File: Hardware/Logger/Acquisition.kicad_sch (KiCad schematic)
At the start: 9 parts, among them J1 Conn_Coaxial, J2 Conn_Coaxial, J3 Conn_Coaxial, J4 Conn_Coaxial, J7 DB9_Female_MountingHoles

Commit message: fix #41
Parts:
- added Q5, Q6, Q7, Q8: BC848, Package_TO_SOT_SMD:SOT-23, symbol Transistor_BJT:BC848
- added R10, R35, R38, R39: 8k2, Resistor_SMD:R_0805_2012Metric, symbol Device:R
- added R36, R37: 100R, Resistor_SMD:R_0805_2012Metric, symbol Device:R
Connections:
- net ANALOG_IN_1: now also Q5.3 (C); no longer R9.2
- net ANALOG_IN_2: now also Q6.3 (C); no longer R100R1.2
- net ANALOG_IN_3: now also Q7.3 (C); no longer R11.2
- net ANALOG_IN_4: now also Q8.3 (C); no longer R12.2
- net EXT_RX: now also R36.1; no longer J7.2
- net EXT_TX: now also R37.1; no longer J7.3
- net GND: now also Q5.2 (E), Q6.2 (E), Q7.2 (E), Q8.2 (E), R10.1, R35.1, R38.1, R39.1
- new net: Q5.1 (B), R10.2, R9.2
- new net: Q6.1 (B), R100R1.2, R35.2
- new net: J7.2, R36.2
- new net: J7.3, R37.2
- new net: Q7.1 (B), R11.2, R38.2
- new net: Q8.1 (B), R12.2, R39.2
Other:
- moved on the sheet: J1, J2, J3, J4, J7, R100R1, R11, R12, R9

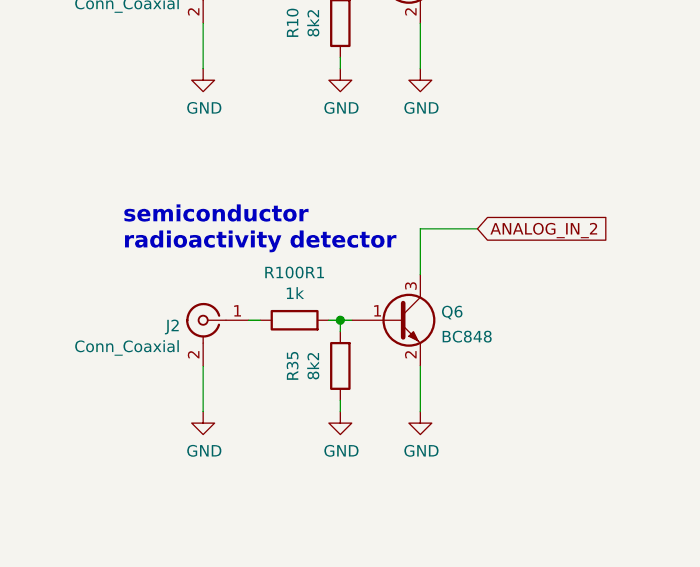
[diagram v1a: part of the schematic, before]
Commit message: cleanup after transition to KiCad6
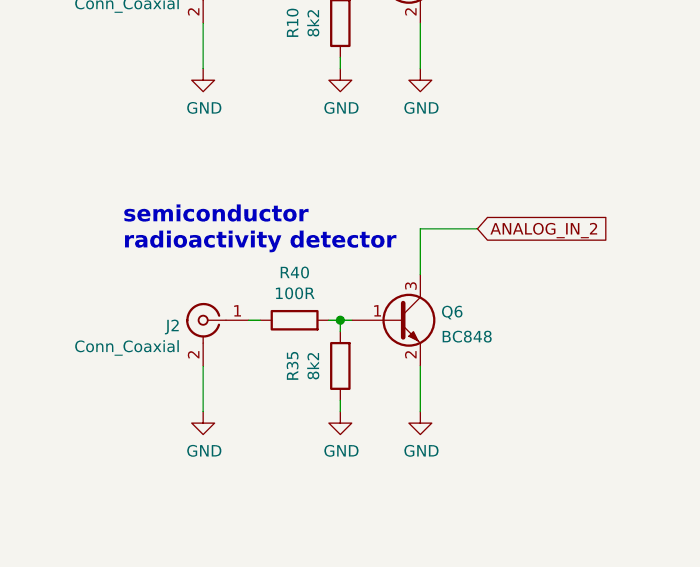
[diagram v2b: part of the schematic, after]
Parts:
- removed R100R1: 1k, Resistor_SMD:R_0805_2012Metric, symbol Device:R
- added R40: 100R, Resistor_SMD:R_0805_2012Metric, symbol Device:R
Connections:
- net at J2.1 (In): now also R40.1
- net at Q6.1 (B), R35.2: now also R40.2
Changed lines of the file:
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@@
   (symbol (lib_id "Device:R") (at 53.34 69.85 90) (unit 1)
     (in_bom yes) (on_board yes)
-    (property "Reference" "R100R1" (id 0) (at 53.34 64.5922 90))
-    (property "Value" "1k" (id 1) (at 53.34 66.9036 90))
+    (property "Reference" "R40" (id 0) (at 53.34 64.5922 90))
+    (property "Value" "100R" (id 1) (at 53.34 66.9036 90))
     (property "Footprint" "Resistor_SMD:R_0805_2012Metric" (id 2) (at 53.34 71.628 90)
       (effects (font (size 1.27 1.27)) hide)

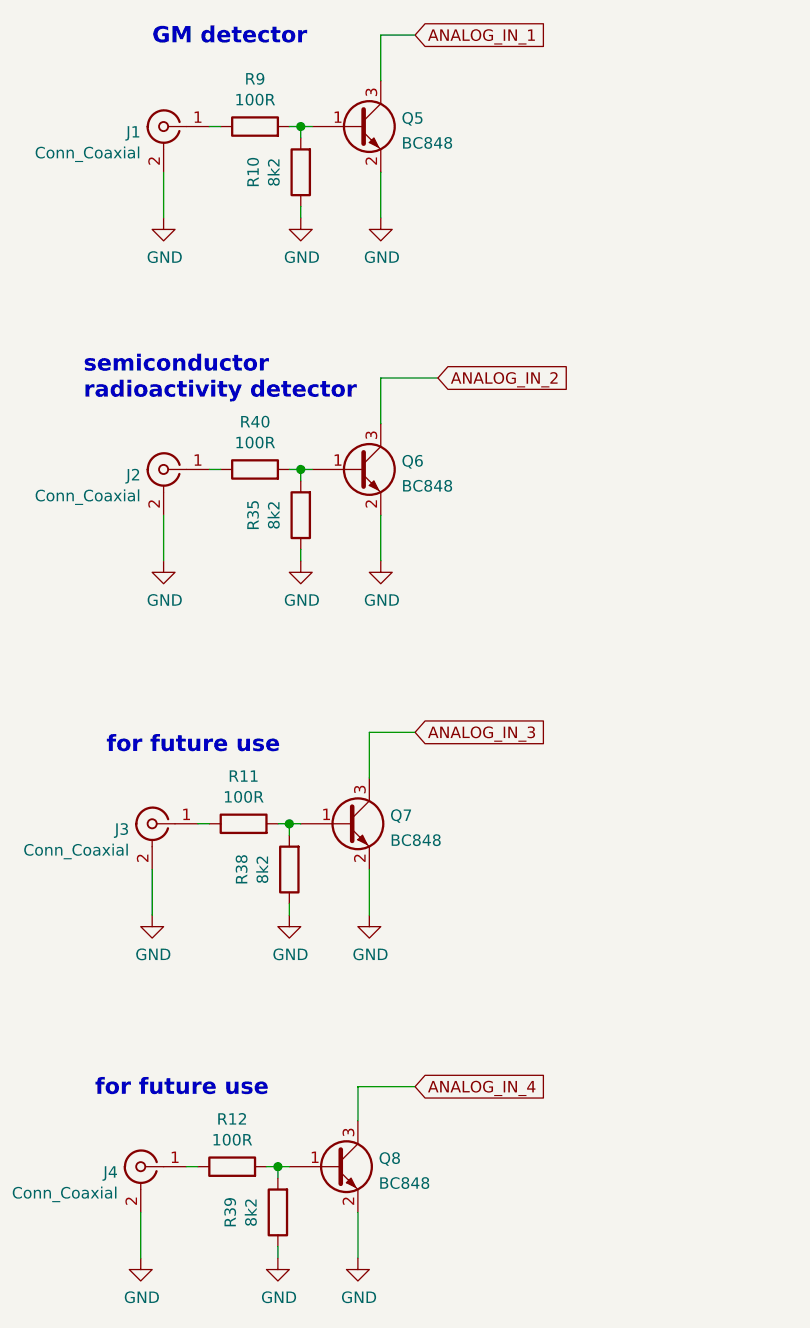
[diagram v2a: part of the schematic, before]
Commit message: apply actual gpio connections to stm32 board, changed photoresistor to phototransistor
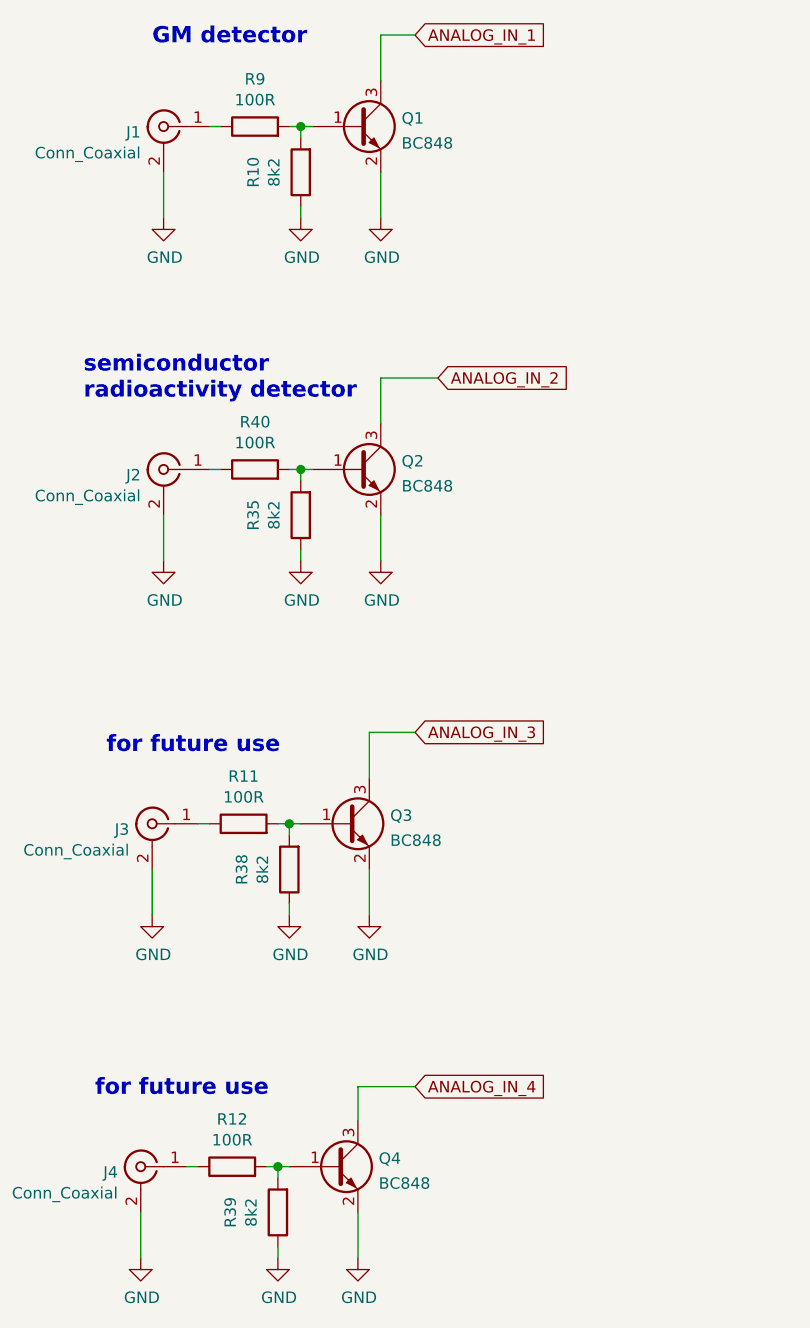
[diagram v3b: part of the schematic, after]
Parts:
- renumbered Q5 to Q1, Q6 to Q2, Q7 to Q3, Q8 to Q4
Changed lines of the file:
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@@
   (symbol (lib_id "Transistor_BJT:BC848") (at 62.23 147.32 0) (unit 1)
     (in_bom yes) (on_board yes) (fields_autoplaced)
-    (property "Reference" "Q8" (id 0) (at 67.0815 146.4115 0)
+    (property "Reference" "Q4" (id 0) (at 67.0815 146.4115 0)
       (effects (font (size 1.27 1.27)) (justify left))
     )
@@
     (pin "3")
   )
-  (symbol (lib_id "Transistor_BJT:BC848") (at 63.5 109.22 0) (unit 1)
+  (symbol (lib_name "Transistor_BJT:BC848_1") (lib_id "Transistor_BJT:BC848") (at 63.5 109.22 0) (unit 1)
     (in_bom yes) (on_board yes) (fields_autoplaced)
-    (property "Reference" "Q7" (id 0) (at 68.3515 108.3115 0)
+    (property "Reference" "Q3" (id 0) (at 68.3515 108.3115 0)
       (effects (font (size 1.27 1.27)) (justify left))
     )
@@
   (symbol (lib_id "Transistor_BJT:BC848") (at 64.77 31.75 0) (unit 1)
     (in_bom yes) (on_board yes) (fields_autoplaced)
-    (property "Reference" "Q5" (id 0) (at 69.6215 30.8415 0)
+    (property "Reference" "Q1" (id 0) (at 69.6215 30.8415 0)
       (effects (font (size 1.27 1.27)) (justify left))
     )
@@
     (pin "3")
   )
-  (symbol (lib_id "Transistor_BJT:BC848") (at 64.77 69.85 0) (unit 1)
+  (symbol (lib_name "Transistor_BJT:BC848_2") (lib_id "Transistor_BJT:BC848") (at 64.77 69.85 0) (unit 1)
     (in_bom yes) (on_board yes) (fields_autoplaced)
-    (property "Reference" "Q6" (id 0) (at 69.6215 68.9415 0)
+    (property "Reference" "Q2" (id 0) (at 69.6215 68.9415 0)
       (effects (font (size 1.27 1.27)) (justify left))
     )

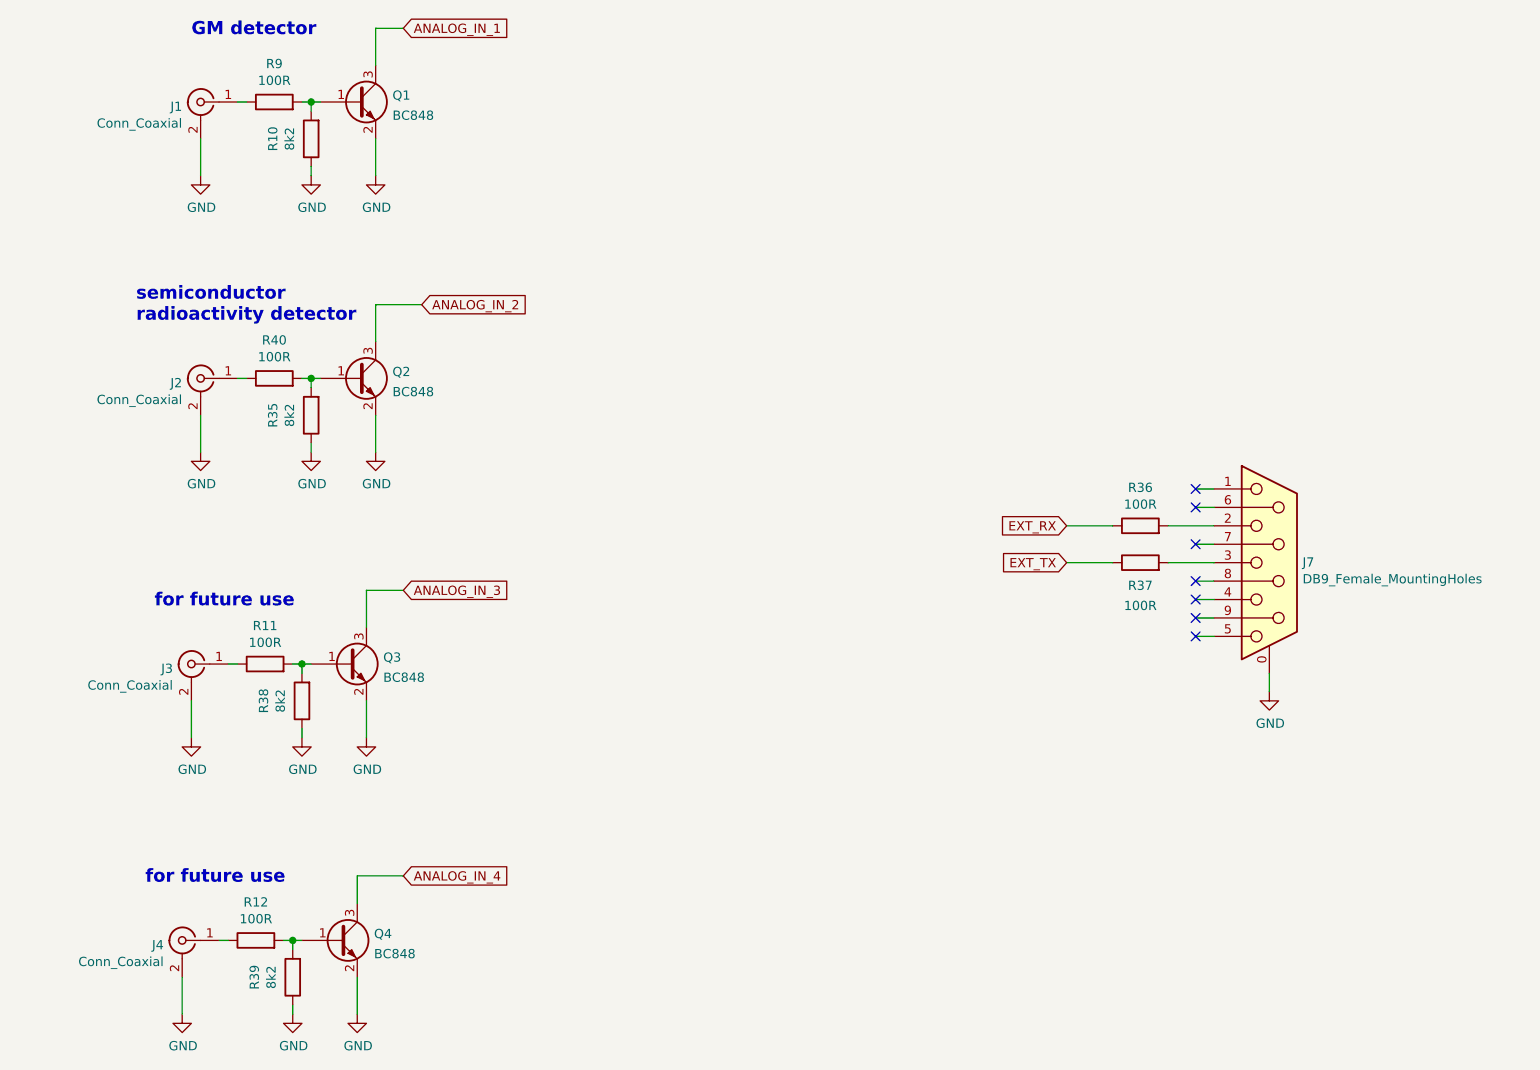
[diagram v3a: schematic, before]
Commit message: draft of rev 3.0, cleanup of repo from not fully open source libs
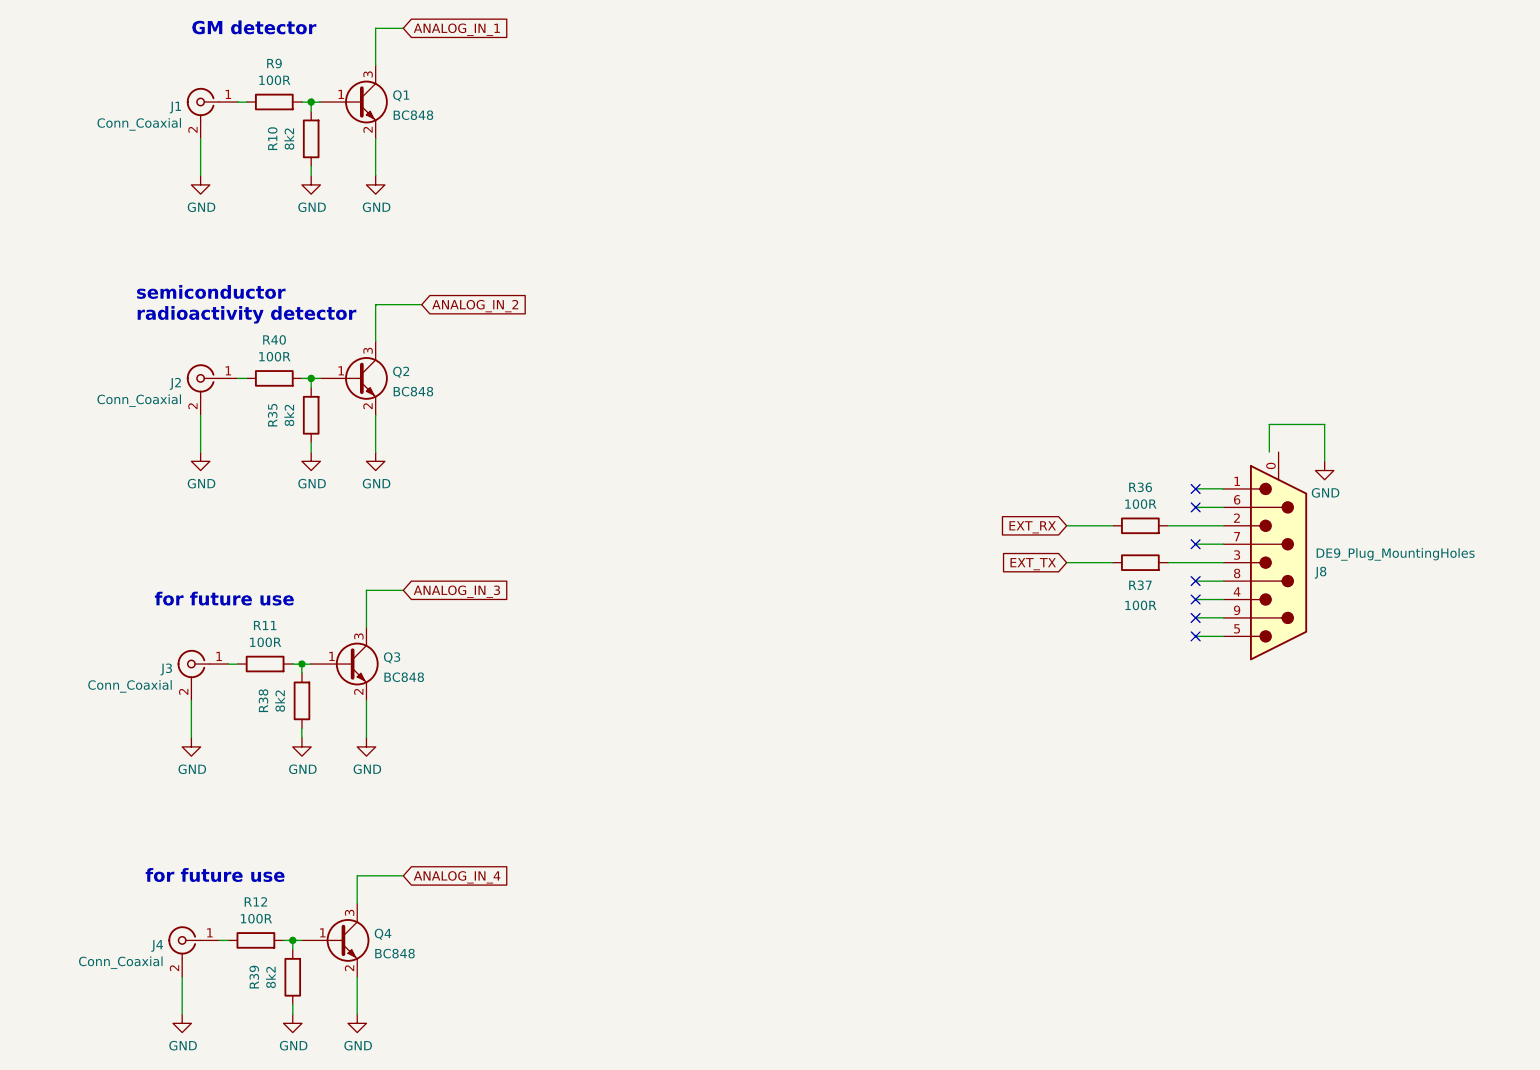
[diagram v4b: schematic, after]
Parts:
- removed J7: DB9_Female_MountingHoles, Connector_Dsub:DSUB-9_Female_Horizontal_P2.77x2.84mm_EdgePinOffset4.94mm_Housed_MountingHolesOffset7.48mm, symbol Connector:DB9_Female_MountingHoles
- added J8: DE9_Plug_MountingHoles, Connector_Dsub:DSUB-9_Female_Horizontal_P2.77x2.84mm_EdgePinOffset4.94mm_Housed_MountingHolesOffset7.48mm, symbol Connector:DE9_Plug_MountingHoles
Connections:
- net at R36.2: now also J8.2
- net at R37.2: now also J8.3
